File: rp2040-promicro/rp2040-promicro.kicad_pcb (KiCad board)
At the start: 2 copper layers, 17.9 x 39.8 mm, 30 parts, among them J2 ProMicro-LeftPin, J3 ProMicro-RightPin, P1 USB2.0_C_12pin, SW1 SW_Push, U1 RP2040, U2 W25Q128JVS, U3 AZ1117-3.3, Y1 Crystal_GND24

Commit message: promicro v2
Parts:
- removed C4: 100nF, rp2040-dev-board:Capacitor_0805_2012
- removed P1: USB2.0_C_12pin, rp2040-dev-board:USB-C-12-Pin-MidMount-ali-v2
- added F1: Polyfuse, $74th:ResettableFuse_KT6-1100SMDI, B.Cu at (59.1, 47.0)
- added J1: USB2.0_C_v3, $74th:USB-C-12-Pin-SMD, F.Cu at (59.0, 47.6)
- added R8: 1kR, rp2040-dev-board:Register_0805_2012, F.Cu at (57.9, 78.4)
- C11, C12: footprint rp2040-dev-board:Capacitor_0603_1608 -> rp2040-dev-board:Capacitor_0805_2012; moved to B.Cu
- C14, C15, C3, C5: moved to B.Cu
- C2: moved to F.Cu
- J2: footprint rp2040-dev-board:LeftPin -> $74th:ProMicro_LIKE_LEFT
- J3: footprint rp2040-dev-board:RightPin -> $74th:ProMicro_LIKE_RIGHT
- SW1: footprint rp2040-dev-board:BOOT -> rp2040-dev-board:SKRPABE010
- U3: footprint rp2040-dev-board:Regulator-AMS1117-SOT-223 -> $74th:Regulator_AMS1117_SOT-89
- Y1: footprint Crystal:Crystal_SMD_3225-4Pin_3.2x2.5mm_HandSoldering -> rp2040-dev-board:Crystal_SMD_3225-4Pin_3.2x2.5mm_HandSoldering; moved to B.Cu
- moved J3 15.4 mm to (66.5, 66.5)
- moved J2 14.0 mm to (51.3, 65.2)
- moved C3 13.6 mm to (62.1, 64.8), turned to 90 degrees
- moved C5 12.8 mm to (56.8, 66.0), turned to 180 degrees
- moved SW1 12.6 mm to (63.0, 56.7), turned to -90 degrees
- moved C15 11.9 mm to (55.2, 59.8), turned to 180 degrees
- moved C9 11.0 mm to (61.2, 67.7), turned to 0 degrees
- moved R1 10.7 mm to (58.3, 63.1)
- moved R2 10.5 mm to (60.2, 63.1)
- moved R5 10.1 mm to (65.6, 48.5)
- moved C1 9.96 mm to (57.4, 68.0), turned to 180 degrees
- moved R3 9.95 mm to (62.7, 57.0), turned to 90 degrees
- moved C10 8.98 mm to (62.8, 74.2), turned to 180 degrees
- moved C12 8.67 mm to (62.6, 78.5)
- moved C8 8.22 mm to (61.9, 71.3)
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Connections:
- C12 pad 2: XOUT -> Net-(C12-Pad2)
- J2 pad 1: 9/RX1 -> 0/TX0
- J2 pad 10: GND -> 7
- J2 pad 11: 1/RX0 -> 8/TX1
- J2 pad 12: 0/TX0 -> 9/RX1
- J2 pad 2: 8/TX1 -> 1/RX0
- J2 pad 3: 7 -> GND
- J2 pad 4: 6 -> GND
- J2 pad 5: 5 -> 2
- J2 pad 6: 4 -> 3
- J2 pad 7: 3 -> 4
- J2 pad 8: 2 -> 5
- J2 pad 9: GND -> 6
- J3 pad 1: +5V -> 21
- J3 pad 10: 20 -> ~{RESET}
- J3 pad 11: 23 -> GND
- J3 pad 12: 21 -> +5V
- J3 pad 2: GND -> 23
- J3 pad 3: ~{RESET} -> 20
- J3 pad 4: +3V3 -> 22
- J3 pad 5: A3 -> A0
- J3 pad 6: A2 -> A1
- J3 pad 7: A1 -> A2
- J3 pad 8: A0 -> A3
- J3 pad 9: 22 -> +3V3
- Y1 pad 3: XOUT -> Net-(C12-Pad2)
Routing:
- net Net-(F1-Pad1): track 0.00 -> 19.9 mm, vias 0 -> 1
- net Net-(R2-Pad1): track 19.8 -> 3.99 mm
- net XOUT: track 16.0 -> 3.15 mm
- net +3V3: track 95.6 -> 83.1 mm, vias 3 -> 14
- net GND: track 29.6 -> 17.9 mm, vias 11 -> 22
- net Net-(R1-Pad1): track 14.7 -> 4.60 mm
- net +1V1: track 22.7 -> 30.5 mm, vias 1 -> 6
- net ~{RESET}: track 26.9 -> 33.7 mm, vias 3 -> 2
- net USB_DM: track 8.45 -> 14.6 mm, vias 2 -> 1
- net XIN: track 10.5 -> 4.81 mm, vias 0 -> 1
- net +5V: track 22.7 -> 17.1 mm, vias 0 -> 1
- net Net-(C12-Pad2): track 0.00 -> 4.99 mm, vias 0 -> 1
- net Net-(R3-Pad1): track 2.10 -> 6.89 mm, vias 0 -> 2
- net Net-(J1-Pad6): track 4.81 -> 8.71 mm
- net QSPI_SS: track 26.9 -> 23.1 mm
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- added copper zone on F.Cu, net +1V1
- added copper zone on F.Cu, net +3V3
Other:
- board size 17.9 x 39.8 mm -> 17.9 x 35.6 mm
- board text added: "RP-ProMicro v2.0.0"
- board text removed: "RP-ProMicro v1.0.1"

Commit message: rp-promicro v2.0.0
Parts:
- moved J3 0.12 mm to (66.6, 66.5)
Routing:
- net 23: track 8.96 -> 10.4 mm
- net GND: track 17.9 -> 19.3 mm
- net A3: track 10.7 -> 9.74 mm
- net +3V3: track 83.1 -> 82.2 mm
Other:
- board size 17.9 x 35.6 mm -> 17.8 x 35.6 mm
- board text added: "0"
- board text added: "1"
- board text added: "2"
- board text added: "20"
- board text added: "21"
- board text added: "22"
- board text added: "23"
- board text added: "26"
- board text added: "27"
- board text added: "28"
- board text added: "29"
- board text added: "3"
- board text added: "3V3"
- board text added: "4"
- board text added: "5"
- board text added: "5V"
- board text added: "6"
- board text added: "7"
- board text added: "8"
- board text added: "9"
- board text added: "A0"
- board text added: "A1"
- board text added: "A2"
- board text added: "A3"
- board text added: "CSn"
- board text added: "G"
- board text added: "I2C1"
- board text added: "RST"
- board text added: "RX"
- board text added: "SCK"
- board text added: "SCL"
- board text added: "SDA"
- board text added: "SPI0"
- board text added: "TX"
- board text added: "UART0"
- board text added: "UART1"
- board text added: "v2.0.0"
- board text removed: "RP-ProMicro v2.0.0"

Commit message: rp-promicro v2.0.0
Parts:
- added REF**: JLCJLCJLCJLC, $74th:JLCJLCJLCJLC, F.Cu at (52.9, 71.6)

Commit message: rp-promicro v2.0.0
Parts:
- U2: footprint rp2040-dev-board:W25Q16-128JV-SOIC -> Package_SO:SOIC-8_5.23x5.23mm_P1.27mm
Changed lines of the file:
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@@
     (descr "RP 2040")
     (tags "Integrated Circuit")
+    (property "MPN" "C2040")
     (property "Sheetfile" "rp2040-promicro.kicad_sch")
     (property "Sheetname" "")
@@
       (net 11 "9{slash}RX1") (pinfunction "9/A9") (pintype "bidirectional"))
   )
-  (footprint "rp2040-dev-board:W25Q16-128JV-SOIC" (layer "F.Cu")
+  (footprint "Package_SO:SOIC-8_5.23x5.23mm_P1.27mm" (layer "F.Cu")
     (at 57.7 62.397)
     (descr "SOIC, 8 Pin (http://www.winbond.com/resource-files/w25q32jv%20revg%2003272018%20plus.pdf#page=68), generated with kicad-footprint-generator ipc_gullwing_generator.py")
@@
     (property "Sheetname" "")
     (attr smd)
-    (fp_text reference "U2" (at -0.842 -4.015) (layer "F.SilkS")
-      (effects (font (size 0.8 0.8) (thickness 0.12)))
+    (fp_text reference "U2" (at 0 -3.56) (layer "F.SilkS")
+      (effects (font (size 1 1) (thickness 0.15)))
     )
     (fp_text value "W25Q128JVS" (at 0 3.56) (layer "F.Fab")
@@
       (effects (font (size 1 1) (thickness 0.15)))
     )
+    (fp_line (start -2.725 -2.725) (end -2.725 -2.465) (layer "F.SilkS") (width 0.12))
+    (fp_line (start 2.725 -2.725) (end 2.725 -2.465) (layer "F.SilkS") (width 0.12))
+    (fp_line (start 0 2.725) (end -2.725 2.725) (layer "F.SilkS") (width 0.12))
+    (fp_line (start -2.725 2.725) (end -2.725 2.465) (layer "F.SilkS") (width 0.12))
+    (fp_line (start -2.725 -2.465) (end -4.4 -2.465) (layer "F.SilkS") (width 0.12))
+    (fp_line (start 0 -2.725) (end -2.725 -2.725) (layer "F.SilkS") (width 0.12))
+    (fp_line (start 0 -2.725) (end 2.725 -2.725) (layer "F.SilkS") (width 0.12))
+    (fp_line (start 0 2.725) (end 2.725 2.725) (layer "F.SilkS") (width 0.12))
     (fp_line (start 2.725 2.725) (end 2.725 2.465) (layer "F.SilkS") (width 0.12))
-    (fp_line (start -2.725 -2.465) (end -4.4 -2.465) (layer "F.SilkS") (width 0.12))
-    (fp_line (start 0 -2.725) (end 2.725 -2.725) (layer "F.SilkS") (width 0.12))
-    (fp_line (start -2.725 2.725) (end -2.725 2.465) (layer "F.SilkS") (width 0.12))
-    (fp_line (start 2.725 -2.725) (end 2.725 -2.465) (layer "F.SilkS") (width 0.12))
-    (fp_line (start 0 -2.725) (end -2.725 -2.725) (layer "F.SilkS") (width 0.12))
-    (fp_line (start 0 2.725) (end -2.725 2.725) (layer "F.SilkS") (width 0.12))
-    (fp_line (start -2.725 -2.725) (end -2.725 -2.465) (layer "F.SilkS") (width 0.12))
-    (fp_line (start 0 2.725) (end 2.725 2.725) (layer "F.SilkS") (width 0.12))
+    (fp_line (start 4.65 2.86) (end 4.65 -2.86) (layer "F.CrtYd") (width 0.05))
+    (fp_line (start -4.65 2.86) (end 4.65 2.86) (layer "F.CrtYd") (width 0.05))
+    (fp_line (start 4.65 -2.86) (end -4.65 -2.86) (layer "F.CrtYd") (width 0.05))
     (fp_line (start -4.65 -2.86) (end -4.65 2.86) (layer "F.CrtYd") (width 0.05))
-    (fp_line (start 4.65 -2.86) (end -4.65 -2.86) (layer "F.CrtYd") (width 0.05))
-    (fp_line (start -4.65 2.86) (end 4.65 2.86) (layer "F.CrtYd") (width 0.05))
-    (fp_line (start 4.65 2.86) (end 4.65 -2.86) (layer "F.CrtYd") (width 0.05))
+    (fp_line (start -2.615 2.615) (end -2.615 -1.615) (layer "F.Fab") (width 0.1))
+    (fp_line (start 2.615 2.615) (end -2.615 2.615) (layer "F.Fab") (width 0.1))
     (fp_line (start -2.615 -1.615) (end -1.615 -2.615) (layer "F.Fab") (width 0.1))
+    (fp_line (start -1.615 -2.615) (end 2.615 -2.615) (layer "F.Fab") (width 0.1))
     (fp_line (start 2.615 -2.615) (end 2.615 2.615) (layer "F.Fab") (width 0.1))
-    (fp_line (start 2.615 2.615) (end -2.615 2.615) (layer "F.Fab") (width 0.1))
-    (fp_line (start -1.6 2.615) (end -1.6 -2.615) (layer "F.Fab") (width 0.1))
-    (fp_line (start -2.615 2.615) (end -2.615 -1.615) (layer "F.Fab") (width 0.1))
-    (fp_line (start -1.615 -2.615) (end 2.615 -2.615) (layer "F.Fab") (width 0.1))
-    (fp_line (start 1.6 2.615) (end 1.6 -2.615) (layer "F.Fab") (width 0.1))
-    (pad "1" smd roundrect (at -3.1 -1.905) (size 2.6 0.6) (layers "F.Cu" "F.Paste" "F.Mask") (roundrect_rratio 0.25)
+    (pad "1" smd roundrect locked (at -3.6 -1.905) (size 1.6 0.6) (layers "F.Cu" "F.Paste" "F.Mask") (roundrect_rratio 0.25)
       (net 1 "QSPI_SS") (pinfunction "~{CS}") (pintype "input"))
-    (pad "2" smd roundrect (at -3.1 -0.635) (size 2.6 0.6) (layers "F.Cu" "F.Paste" "F.Mask") (roundrect_rratio 0.25)
+    (pad "2" smd roundrect locked (at -3.6 -0.635) (size 1.6 0.6) (layers "F.Cu" "F.Paste" "F.Mask") (roundrect_rratio 0.25)
       (net 2 "QSPI_SD1") (pinfunction "DO(IO1)") (pintype "bidirectional"))
-    (pad "3" smd roundrect (at -3.1 0.635) (size 2.6 0.6) (layers "F.Cu" "F.Paste" "F.Mask") (roundrect_rratio 0.25)
+    (pad "3" smd roundrect locked (at -3.6 0.635) (size 1.6 0.6) (layers "F.Cu" "F.Paste" "F.Mask") (roundrect_rratio 0.25)
       (net 3 "QSPI_SD2") (pinfunction "IO2") (pintype "bidirectional"))
-    (pad "4" smd roundrect (at -3.1 1.905) (size 2.6 0.6) (layers "F.Cu" "F.Paste" "F.Mask") (roundrect_rratio 0.25)
-      (net 4 "GND") (pinfunction "GND") (pintype "power_in") (zone_connect 2))
-    (pad "5" smd roundrect (at 3.1 1.905) (size 2.6 0.6) (layers "F.Cu" "F.Paste" "F.Mask") (roundrect_rratio 0.25)
+    (pad "4" smd roundrect locked (at -3.6 1.905) (size 1.6 0.6) (layers "F.Cu" "F.Paste" "F.Mask") (roundrect_rratio 0.25)
+      (net 4 "GND") (pinfunction "GND") (pintype "power_in"))
+    (pad "5" smd roundrect locked (at 3.6 1.905) (size 1.6 0.6) (layers "F.Cu" "F.Paste" "F.Mask") (roundrect_rratio 0.25)
       (net 5 "QSPI_SD0") (pinfunction "DI(IO0)") (pintype "bidirectional"))
-    (pad "6" smd roundrect (at 3.1 0.635) (size 2.6 0.6) (layers "F.Cu" "F.Paste" "F.Mask") (roundrect_rratio 0.25)
+    (pad "6" smd roundrect locked (at 3.6 0.635) (size 1.6 0.6) (layers "F.Cu" "F.Paste" "F.Mask") (roundrect_rratio 0.25)
       (net 6 "QSPI_CLK") (pinfunction "CLK") (pintype "input"))
-    (pad "7" smd roundrect (at 3.1 -0.635) (size 2.6 0.6) (layers "F.Cu" "F.Paste" "F.Mask") (roundrect_rratio 0.25)
+    (pad "7" smd roundrect locked (at 3.6 -0.635) (size 1.6 0.6) (layers "F.Cu" "F.Paste" "F.Mask") (roundrect_rratio 0.25)
       (net 7 "QSPI_SD3") (pinfunction "IO3") (pintype "bidirectional"))
-    (pad "8" smd roundrect (at 3.1 -1.905) (size 2.6 0.6) (layers "F.Cu" "F.Paste" "F.Mask") (roundrect_rratio 0.25)
+    (pad "8" smd roundrect locked (at 3.6 -1.905) (size 1.6 0.6) (layers "F.Cu" "F.Paste" "F.Mask") (roundrect_rratio 0.25)
       (net 45 "+3V3") (pinfunction "VCC") (pintype "power_in"))
-    (model "${KICAD6_3DMODEL_DIR}/Package_SO.3dshapes/SOIC-8_5.275x5.275mm_P1.27mm.wrl"
+    (model "${KICAD6_3DMODEL_DIR}/Package_SO.3dshapes/SOIC-8_5.23x5.23mm_P1.27mm.wrl"
       (offset (xyz 0 0 0))
       (scale (xyz 1 1 1))

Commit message: rp-promicro v2.0.0
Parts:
- U2: footprint Package_SO:SOIC-8_5.23x5.23mm_P1.27mm -> $74th:W25Q16-128JV-SOIC

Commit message: rp2040-promicro/2.0.1
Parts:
- added G***: LOGO, $74th:74th-3mm, B.Cu at (64.5, 54.3)
- added REF**: twitter, $74th:twitter, F.Cu at (55.9, 56.8)
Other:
- board text added: "2DA"
- board text added: "3CL"
- board text added: "v2.0.1"
- board text removed: "2"
- board text removed: "3"
- board text removed: "SCL"
- board text removed: "SDA"
- board text removed: "v2.0.0"

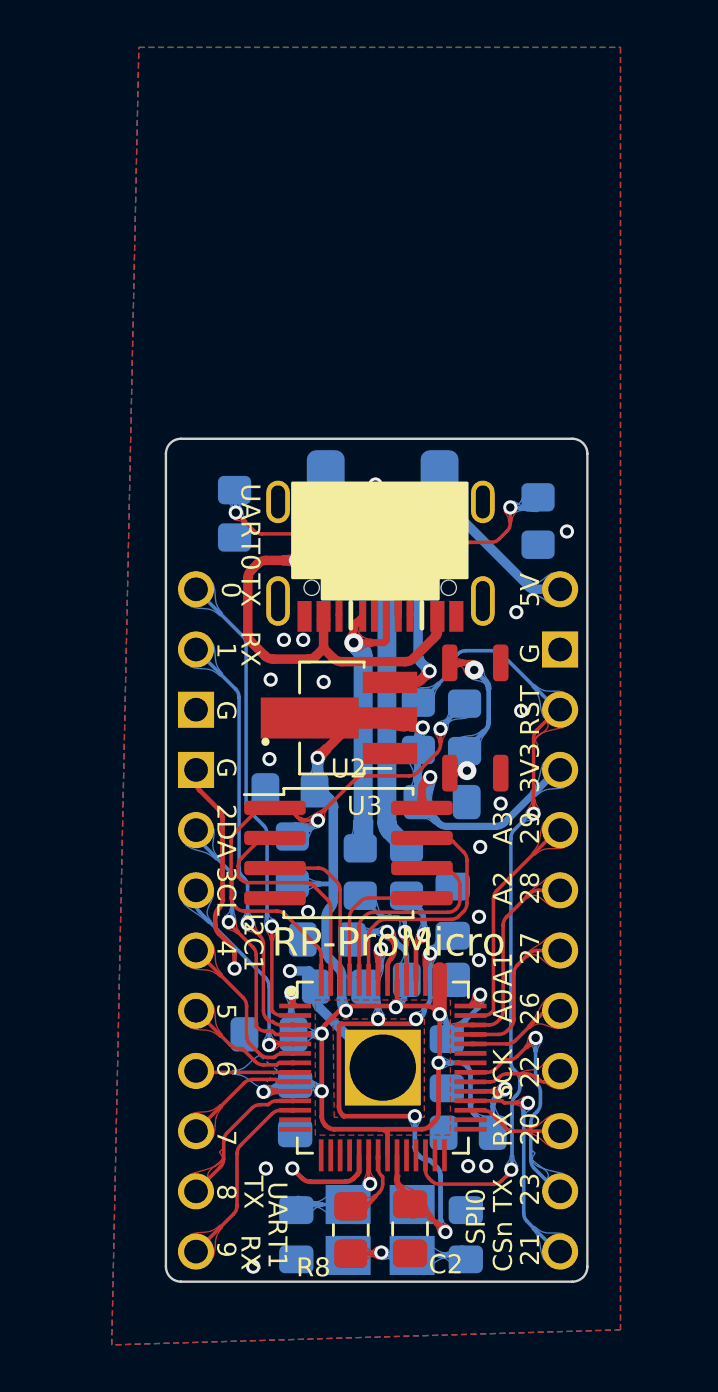
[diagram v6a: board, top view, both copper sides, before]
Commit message: v2.0.1で最後に位置を整列したのが未コミットだった
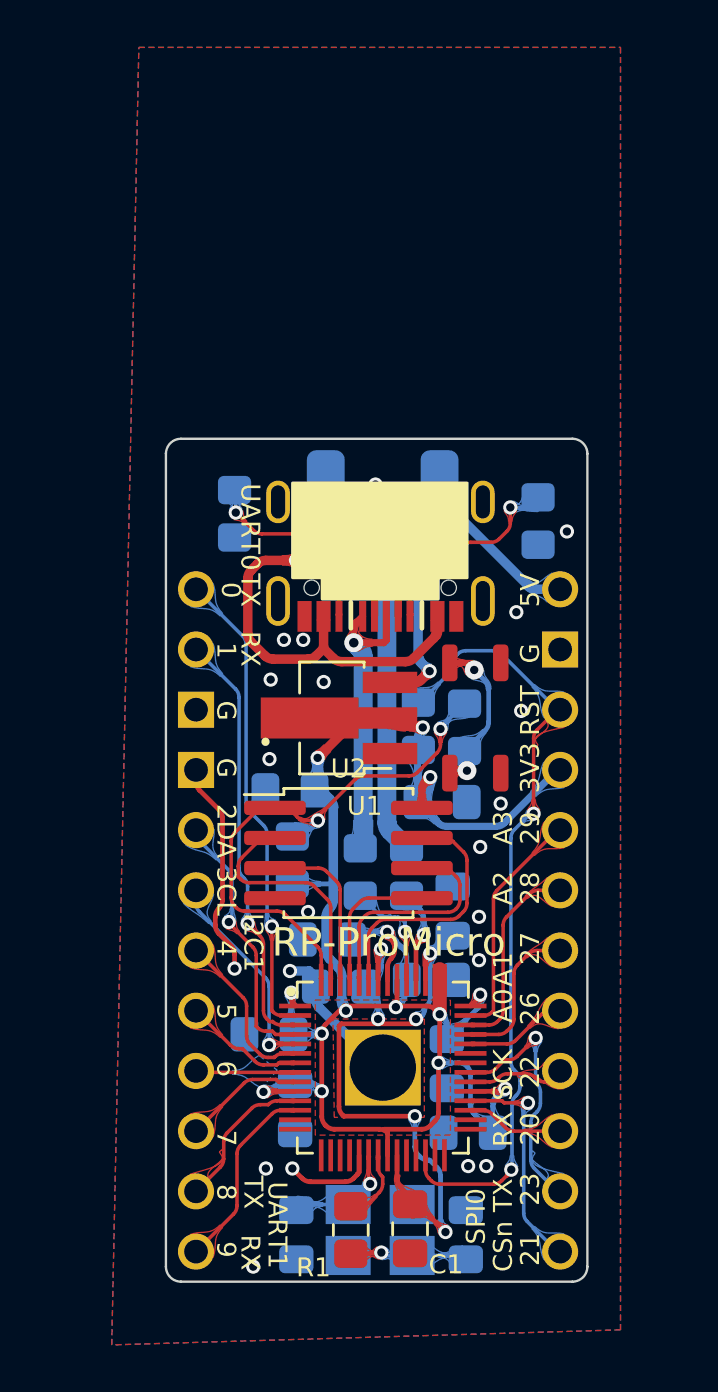
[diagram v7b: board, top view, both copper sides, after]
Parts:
- renumbered C2 to C1, C8 to C10, C7 to C11, C10 to C12, C12 to C13, C11 to C14, C14 to C2, C15 to C3, C13 to C4, C3 to C5, C5 to C6, C9 to C7, C1 to C8, C6 to C9, R8 to R1, R4 to R2, R5 to R3, R3 to R4, R7 to R5, R2 to R7, R1 to R8, U3 to U1, U1 to U3

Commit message: rp2040-promicro/2.0.2
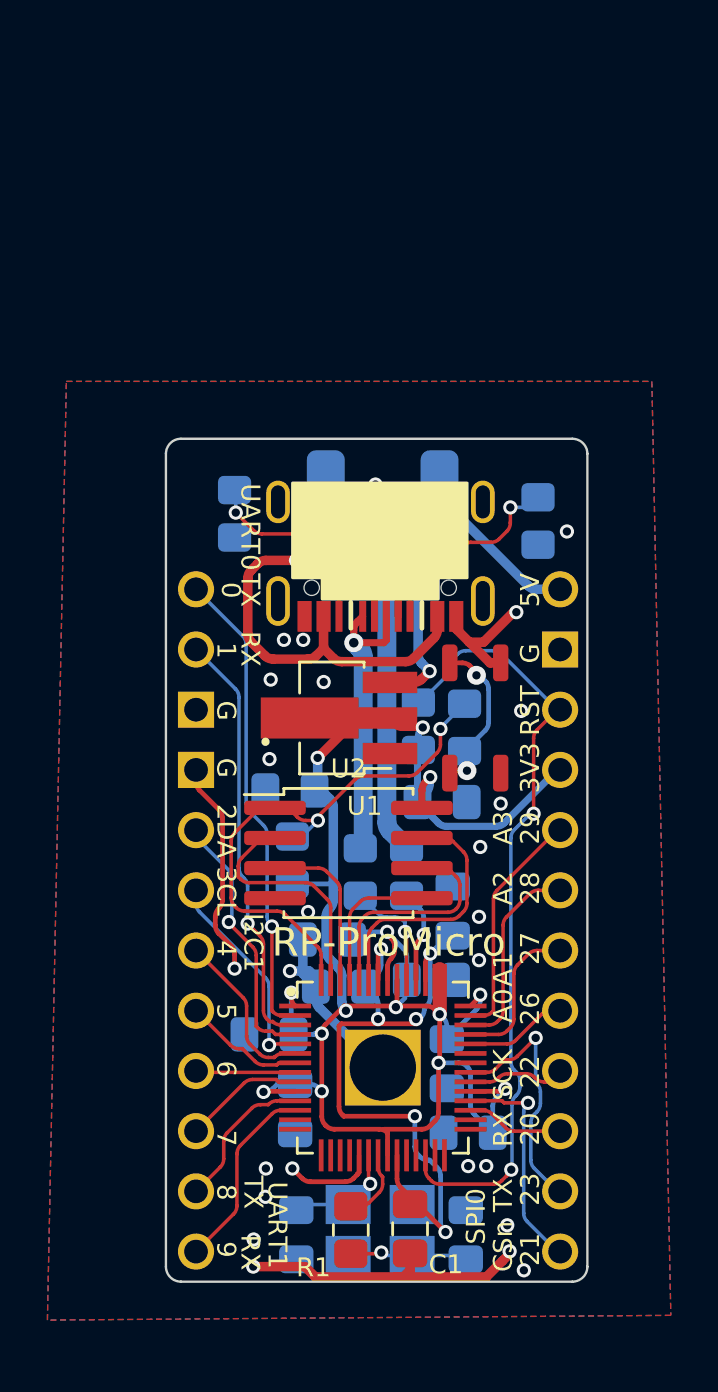
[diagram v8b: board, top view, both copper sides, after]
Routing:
- net GND: track 19.3 -> 39.9 mm, vias 22 -> 27
- removed copper zone on F.Cu, net +1V1
- removed copper zone on F.Cu, net +3V3
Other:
- board text added: "${REVISION}"
- board text removed: "v2.0.1"
